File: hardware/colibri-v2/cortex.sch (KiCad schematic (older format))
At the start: 54 parts

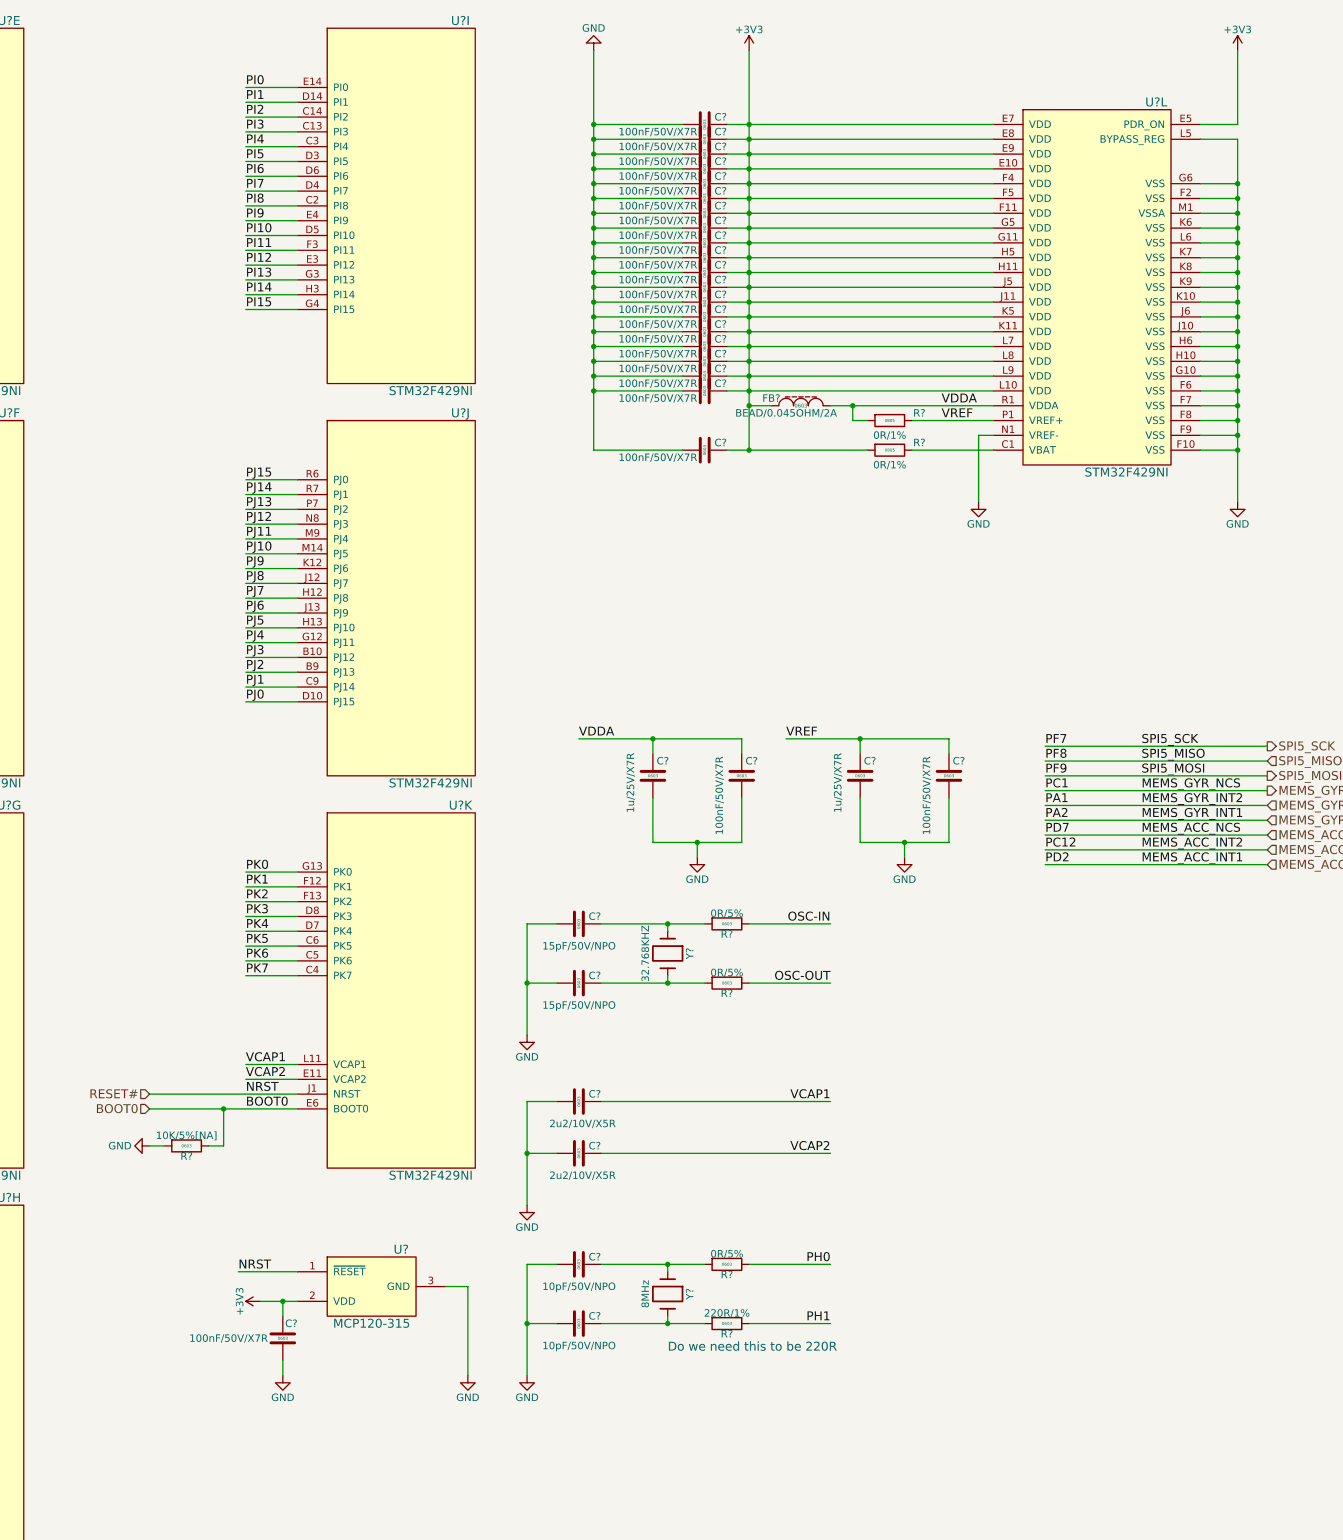
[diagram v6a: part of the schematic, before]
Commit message: Added voltage monitor TLV803SDBZT
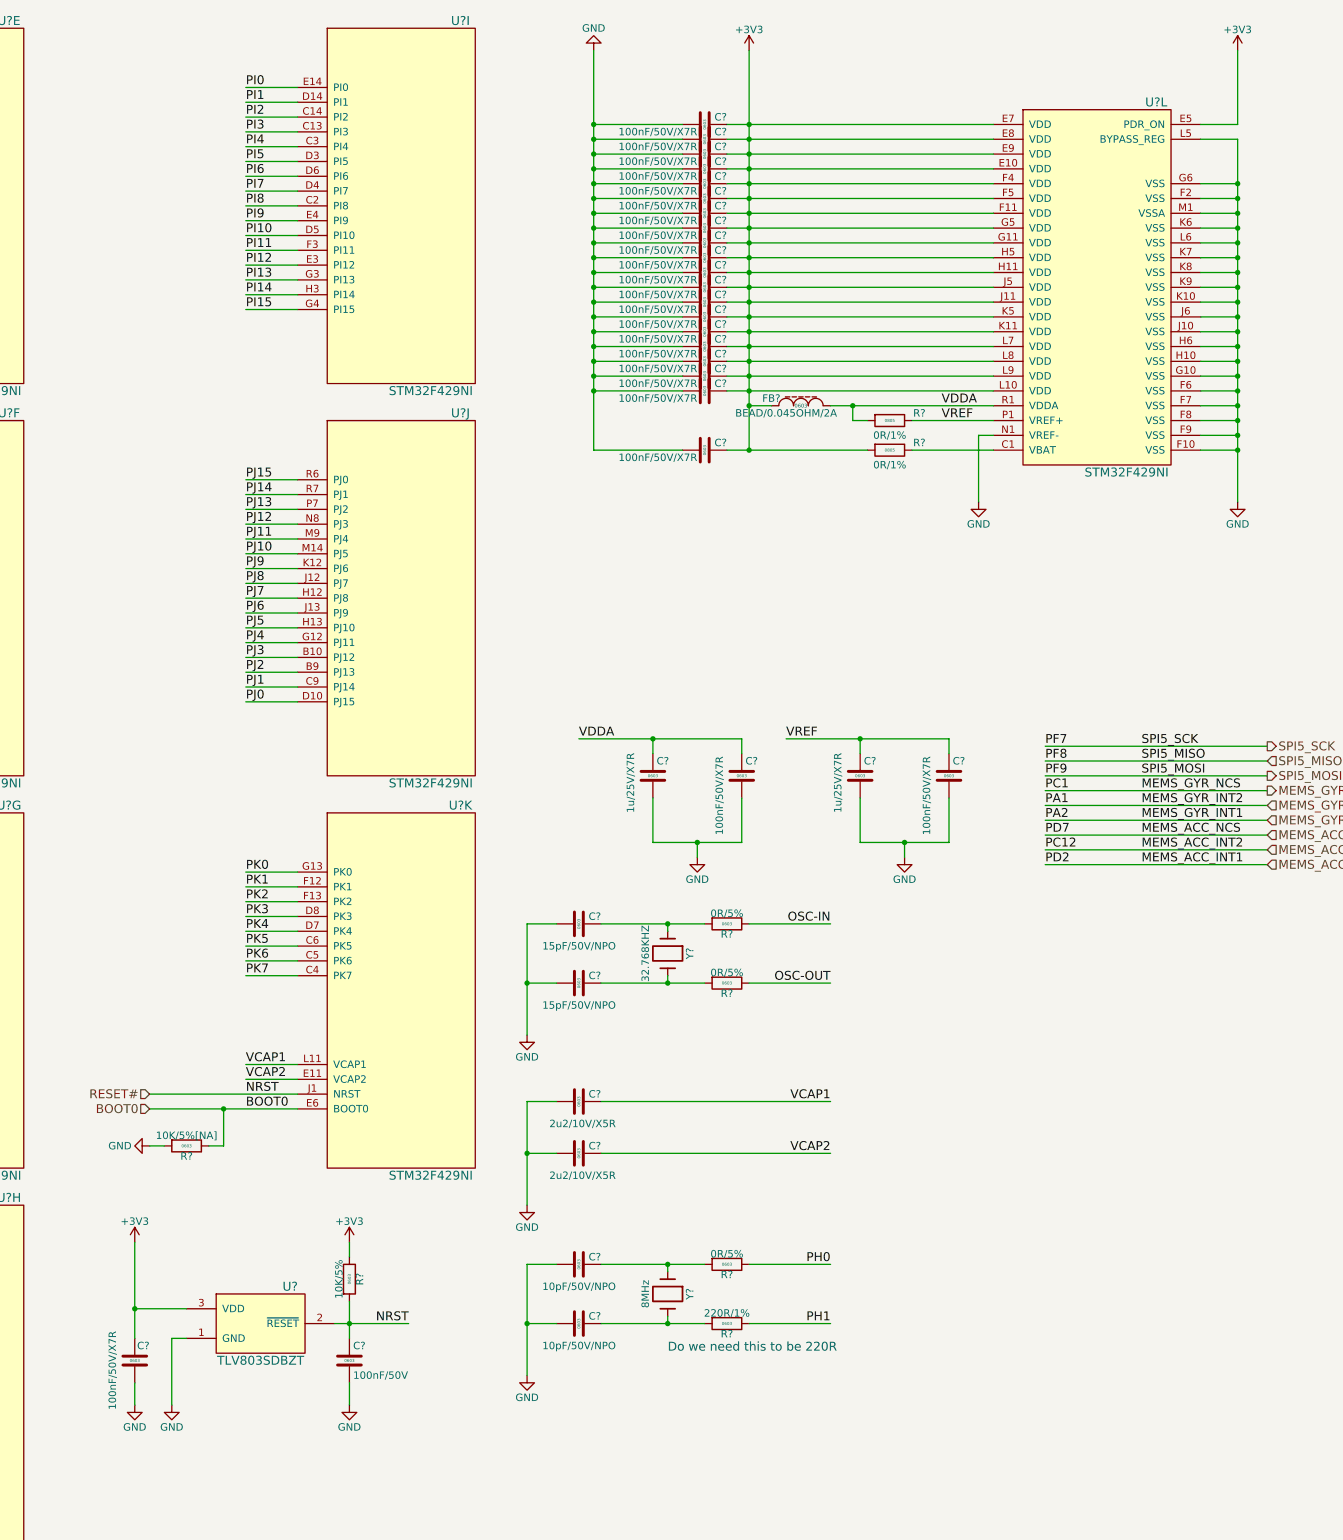
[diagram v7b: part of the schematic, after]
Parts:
- removed U?: MCP120-315, TO_SOT_Packages_SMD:SOT-23, symbol MCP120/130
- added C?: 100nF/50V, Capacitors_SMD:C_0603, symbol C_SMT
- added R?: 10K/5%, Resistors_SMD:R_0603, symbol R_SMT
- added U?: TLV803SDBZT, TO_SOT_Packages_SMD:SOT-23, symbol TLV803
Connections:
- net +3V3: now also R?.1, U?.3 (VDD)
- net GND: now also C?.2, U?.1 (GND)
- net RESET#: now also C?.1, R?.2, U?.2 (~RESET)
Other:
- moved on the sheet: C?
